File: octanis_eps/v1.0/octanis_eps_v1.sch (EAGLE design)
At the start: 153 parts, among them IC1 OPA2333DGK, Q1 32.768kHz, Q100 BSS123, Q2 BSC0901NS, U1 CSD16327Q3_DQG_8, U10 CSD16327Q3_DQG_8, U11 CSD16327Q3_DQG_8, U12 TPS630250YFFT, U15 MSP430FR5969, U2 CSD16327Q3_DQG_8, U3 CSD16327Q3_DQG_8, U5 TPS2022D, U6 TPS630250YFFT, U7 TPS630250YFFT, U8 TPS61232, U9 BQ24650_RVA_16

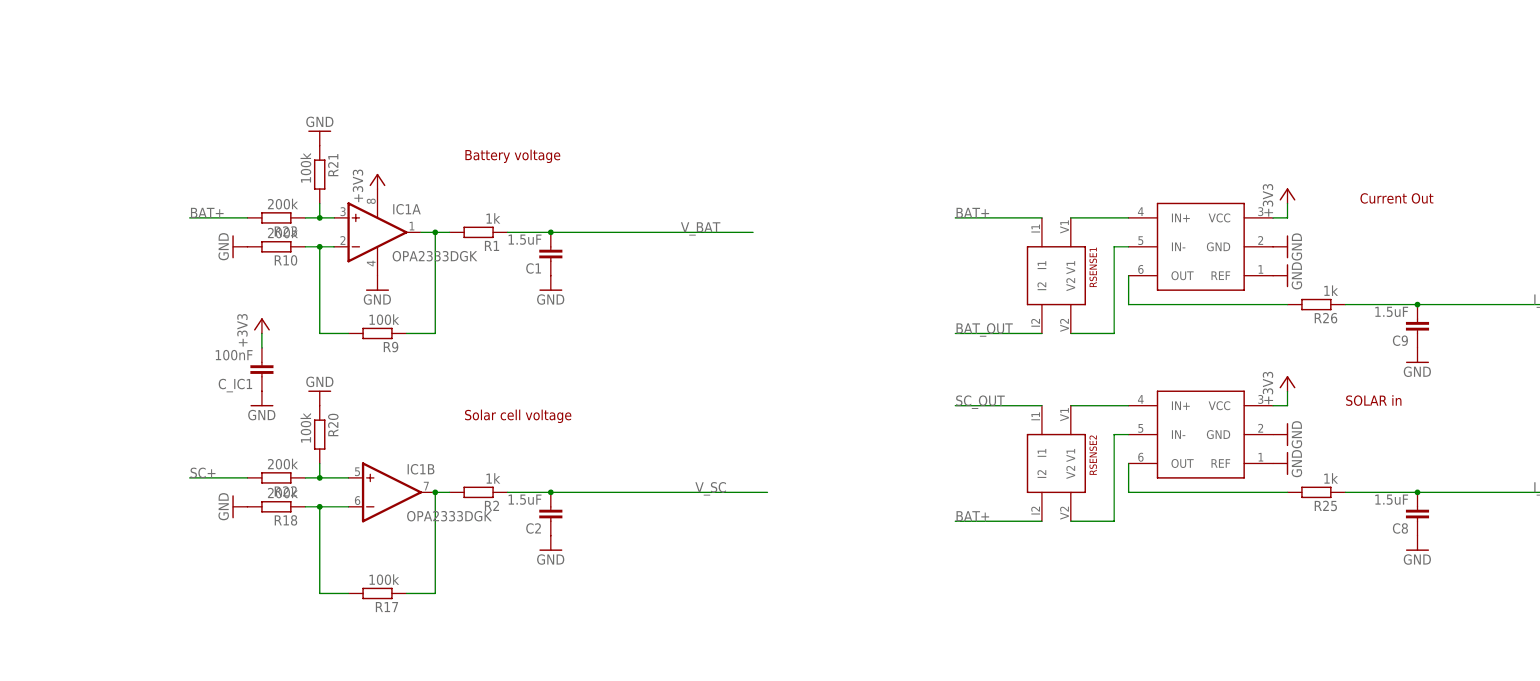
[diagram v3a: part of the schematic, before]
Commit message: dru check; added proper grounding and AVCC for all amps
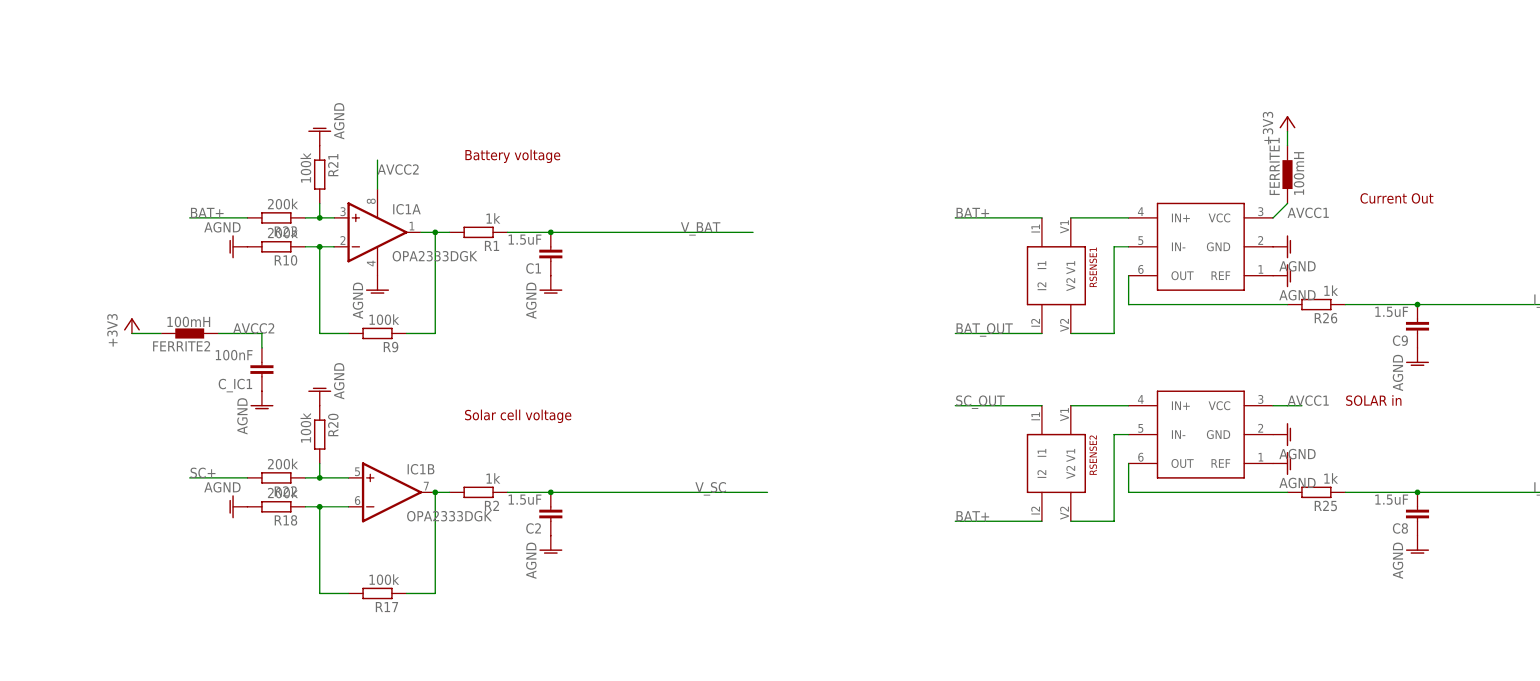
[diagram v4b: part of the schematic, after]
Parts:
- added FERRITE1, FERRITE2: 100mH, inductors:BLM15HD601SN1
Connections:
- new net AVCC1: FERRITE1.1, U$2.VCC, U$3.VCC
- new net AVCC2: C_IC1.2, FERRITE2.1, IC1P.V+
- net +3V3: now also FERRITE1.2, FERRITE2.2; no longer C_IC1.2, IC1P.V+, U$2.VCC, U$3.VCC
- net AGND: now also C1.1, C2.1, C8.1, C9.1, C_IC1.1, IC1P.V-, R10.2, R18.2, R20.1, R21.1, U$2.GND, U$2.REF, U$3.GND, U$3.REF
- net GND: no longer C1.1, C2.1, C8.1, C9.1, C_IC1.1, IC1P.V-, R10.2, R18.2, R20.1, R21.1, U$2.GND, U$2.REF, U$3.GND, U$3.REF

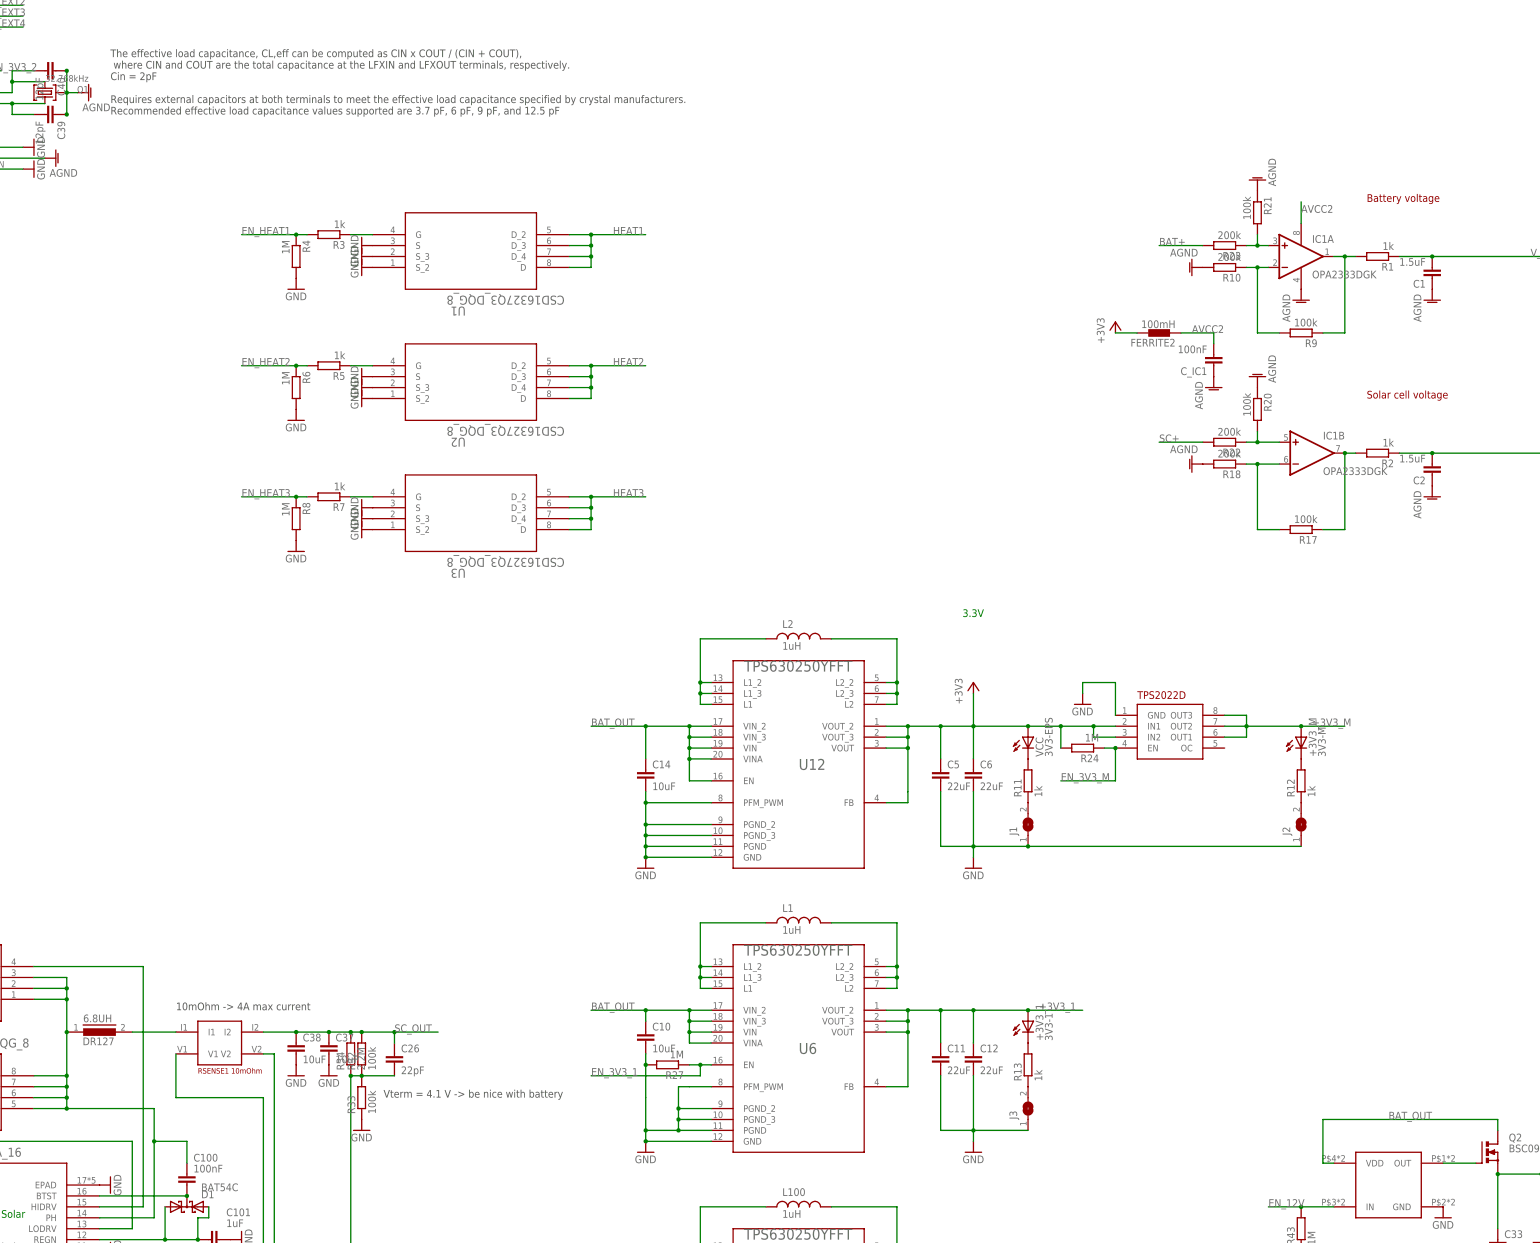
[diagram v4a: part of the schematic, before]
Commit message: removed ground loops
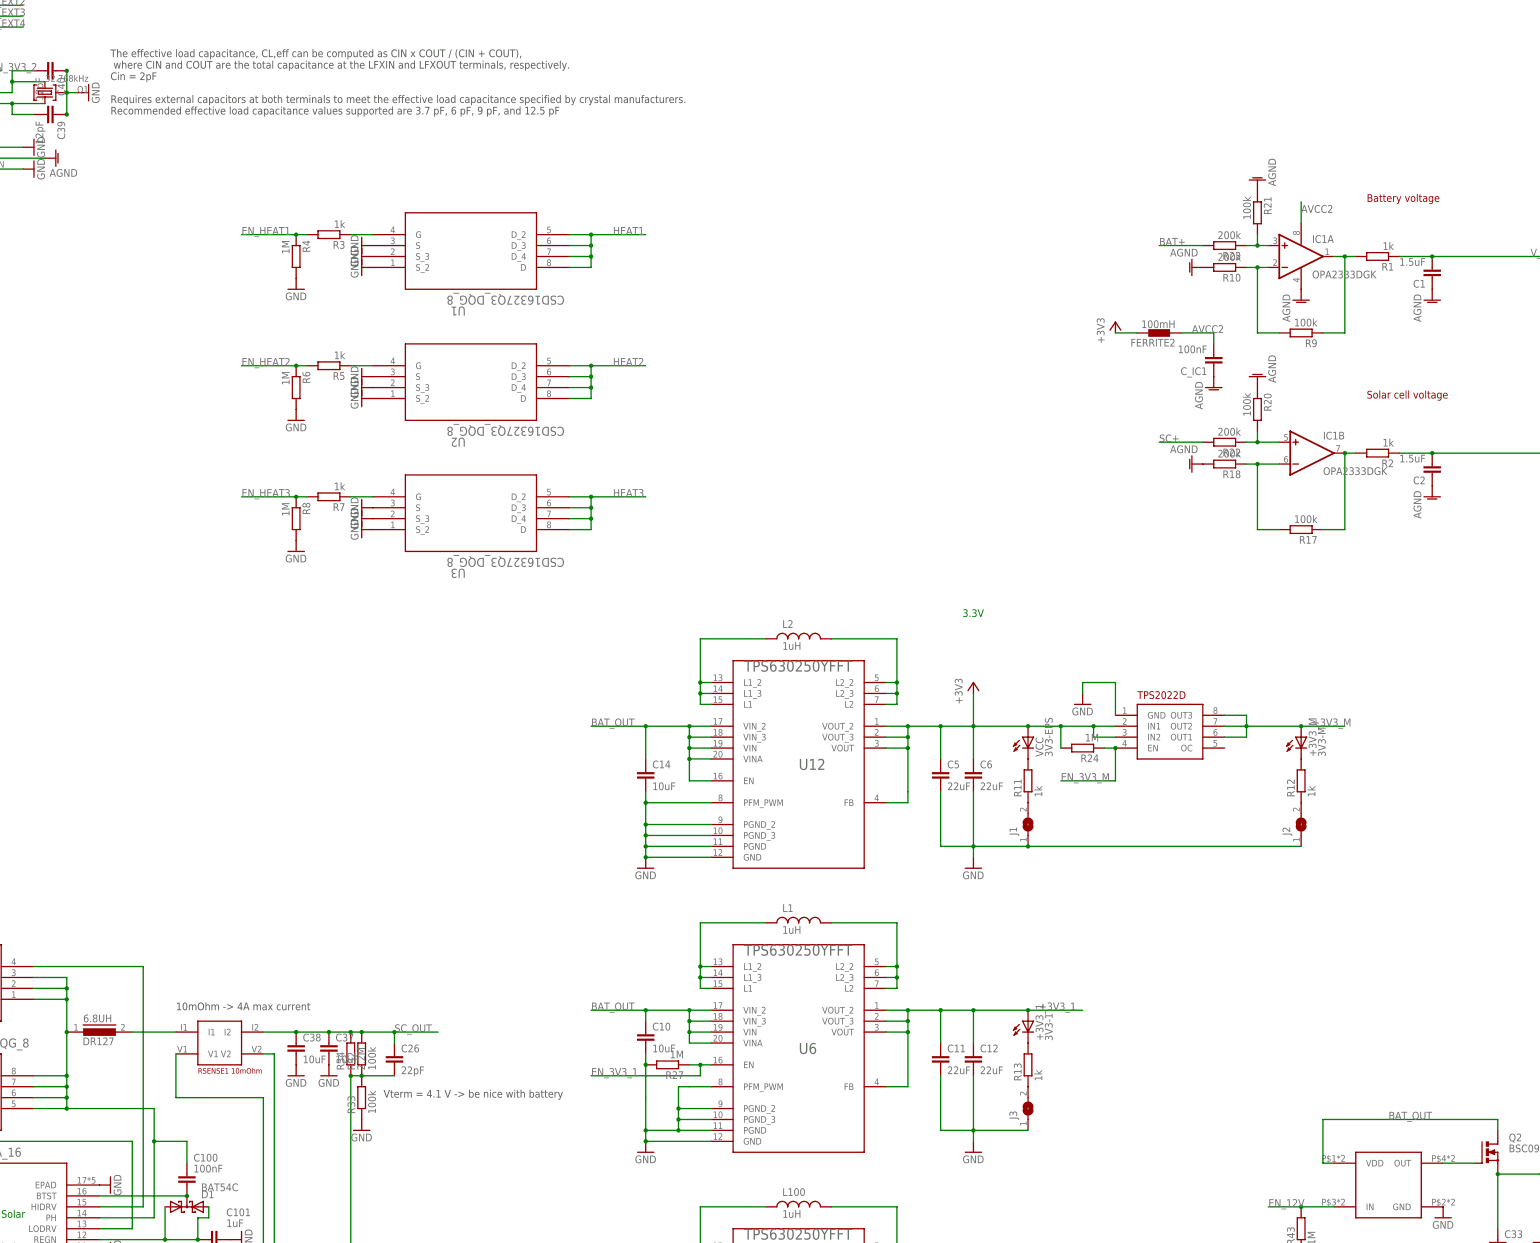
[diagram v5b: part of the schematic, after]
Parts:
- removed U$4: MIC4414, Octanis1_EPS:MIC4414
- added U$5: MIC5019, Octanis1_EPS:MIC5019
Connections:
- net AGND: no longer C39.1, C40.1, Q1.GND
- net BAT_OUT: now also U$5.VDD; no longer U$4.VDD
- net EN_12V: now also U$5.IN; no longer U$4.IN
- net GND: now also C39.1, C40.1, Q1.GND, U$5.GND; no longer U$4.GND
- net N$10: now also U$5.OUT; no longer U$4.OUT
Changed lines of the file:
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@@
 <part name="AGND6" library="supply1" deviceset="AGND" device=""/>
 <part name="AGND7" library="supply1" deviceset="AGND" device=""/>
-<part name="AGND8" library="supply1" deviceset="AGND" device=""/>
 <part name="AGND9" library="supply1" deviceset="AGND" device=""/>
-<part name="U$4" library="Octanis1_EPS" deviceset="MIC4414" device=""/>
 <part name="GND10" library="supply1" deviceset="GND" device=""/>
 <part name="R43" library="rcl" deviceset="R-EU_" device="R0603" value="1M"/>
@@
 <part name="AGND24" library="supply1" deviceset="AGND" device=""/>
 <part name="FERRITE2" library="inductors" deviceset="BLM15H" device="" technology="D601SN1" value="100mH"/>
+<part name="U$5" library="Octanis1_EPS" deviceset="MIC5019" device=""/>
+<part name="GND24" library="supply1" deviceset="GND" device=""/>
 </parts>
 <sheets>
@@
 <instance part="AGND6" gate="VR1" x="43.18" y="180.34" rot="R90"/>
 <instance part="AGND7" gate="VR1" x="160.02" y="307.34" rot="R90"/>
-<instance part="AGND8" gate="VR1" x="167.64" y="322.58" rot="R90"/>
 <instance part="AGND9" gate="VR1" x="132.08" y="375.92" rot="R90"/>
-<instance part="U$4" gate="G$1" x="469.9" y="68.58"/>
 <instance part="GND10" gate="1" x="482.6" y="60.96"/>
 <instance part="R43" gate="G$1" x="449.58" y="58.42" rot="R90"/>
@@
 <instance part="AGND24" gate="VR1" x="609.6" y="243.84" rot="R90"/>
 <instance part="FERRITE2" gate="G$1" x="416.56" y="266.7" rot="R180"/>
+<instance part="U$5" gate="G$1" x="469.9" y="68.58"/>
+<instance part="GND24" gate="1" x="167.64" y="322.58" rot="R90"/>
 </instances>
 <busses>
@@
 </segment>
 <segment>
-<pinref part="U$4" gate="G$1" pin="GND"/>
-<pinref part="GND10" gate="1" pin="GND"/>
-</segment>
-<segment>
 <pinref part="R43" gate="G$1" pin="1"/>
 <pinref part="GND70" gate="1" pin="GND"/>
+</segment>
+<segment>
+<pinref part="GND10" gate="1" pin="GND"/>
+<pinref part="U$5" gate="G$1" pin="GND"/>
+</segment>
+<segment>
+<pinref part="Q1" gate="&gt;NAME" pin="GND"/>
+<wire x1="165.1" y1="322.58" x2="162.56" y2="322.58" width="0.1524" layer="91"/>
+<pinref part="C39" gate="G$1" pin="1"/>
+<wire x1="162.56" y1="317.5" x2="162.56" y2="322.58" width="0.1524" layer="91"/>
+<pinref part="C40" gate="G$1" pin="1"/>
+<wire x1="162.56" y1="322.58" x2="162.56" y2="327.66" width="0.1524" layer="91"/>
+<junction x="162.56" y="322.58"/>
+<junction x="162.56" y="317.5"/>
+<junction x="162.56" y="327.66"/>
+<pinref part="GND24" gate="1" pin="GND"/>
 </segment>
 </net>
@@
 <net name="EN_12V" class="0">
 <segment>
-<pinref part="U$4" gate="G$1" pin="IN"/>
 <wire x1="457.2" y1="63.5" x2="449.58" y2="63.5" width="0.1524" layer="91"/>
 <label x="441.96" y="63.5" size="1.778" layer="95"/>
@@
 <wire x1="449.58" y1="63.5" x2="441.96" y2="63.5" width="0.1524" layer="91"/>
 <junction x="449.58" y="63.5"/>
+<pinref part="U$5" gate="G$1" pin="IN"/>
 </segment>
 <segment>
@@
 <wire x1="495.3" y1="83.82" x2="454.66" y2="83.82" width="0.1524" layer="91"/>
 <wire x1="454.66" y1="83.82" x2="454.66" y2="73.66" width="0.1524" layer="91"/>
-<pinref part="U$4" gate="G$1" pin="VDD"/>
 <wire x1="454.66" y1="73.66" x2="457.2" y2="73.66" width="0.1524" layer="91"/>
 <label x="469.9" y="83.82" size="1.778" layer="95"/>
+<pinref part="U$5" gate="G$1" pin="VDD"/>
 </segment>
 </net>
@@
 </segment>
 <segment>
-<pinref part="Q1" gate="&gt;NAME" pin="GND"/>
-<wire x1="165.1" y1="322.58" x2="162.56" y2="322.58" width="0.1524" layer="91"/>
-<pinref part="C39" gate="G$1" pin="1"/>
-<wire x1="162.56" y1="317.5" x2="162.56" y2="322.58" width="0.1524" layer="91"/>
-<pinref part="C40" gate="G$1" pin="1"/>
-<wire x1="162.56" y1="322.58" x2="162.56" y2="327.66" width="0.1524" layer="91"/>
-<junction x="162.56" y="322.58"/>
-<junction x="162.56" y="317.5"/>
-<junction x="162.56" y="327.66"/>
-<pinref part="AGND8" gate="VR1" pin="AGND"/>
-</segment>
-<segment>
 <pinref part="C3" gate="G$1" pin="2"/>
 <wire x1="129.54" y1="375.92" x2="127" y2="375.92" width="0.1524" layer="91"/>
@@
 <segment>
 <pinref part="Q2" gate="G$1" pin="G"/>
-<pinref part="U$4" gate="G$1" pin="OUT"/>
 <wire x1="482.6" y1="73.66" x2="490.22" y2="73.66" width="0.1524" layer="91"/>
-</segment>
-</net>
+<pinref part="U$5" gate="G$1" pin="OUT"/>
+</segment>
+</net>
